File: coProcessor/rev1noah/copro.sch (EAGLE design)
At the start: 0 parts

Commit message: added several eagle libraries, all "big" parts are on the copro schematic
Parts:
- added J1: USB_MINI-B_SMT, SparkFun-Connectors:USB_MINI-B_SMT
- added J2: PJ-002AH-SMT-TR, PJ-002AH-SMT-TR:PJ-002AH-SMT-TR
- added J3: 455-1750-1-ND, SparkFun-Connectors:CONN_03
- added J4: 30320-6002HB, 30320-6002HB:30320-6002HB
- added OK1: SFH610, optocoupler:SFH610
- added P1: 503500-0991, 503500-0991:503500-0991
- added P2: 39-30-02, con-molex-mini-fit:39-30-02
- added U$1: 5530843, 5530843-6:5530843
- added U$2: STM32F4V_100PIN_GENERIC, stm32f4:STM32F4V_100PIN_GENERIC
- added U$3: DF13-4P-1.25DSA, con-hirose-df13:DF13-4P-1.25DSA
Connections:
- new net GND: U$1.GND_1, U$1.GND_2, U$1.GND_3, U$1.GND_4, U$1.GND_5, U$1.GND_6
- new net N$1: U$1.3.3V_1, U$1.3.3V_2, U$1.3.3V_3
- new net POWER: U$1.3.3V_4, U$1.3.3V_5, U$1.3.3V_6

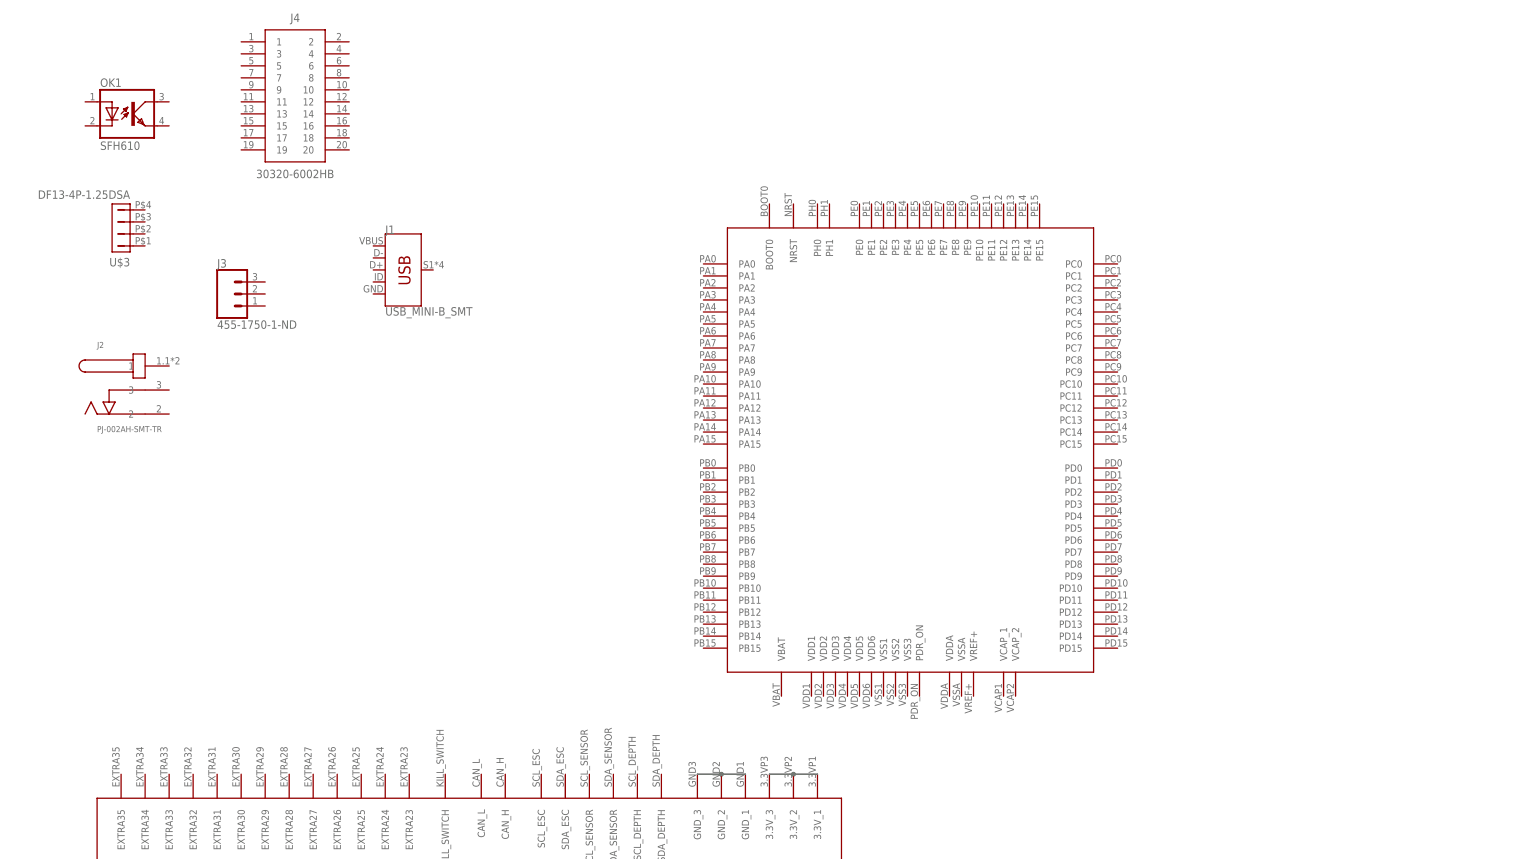
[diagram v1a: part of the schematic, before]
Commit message: some progress on the copro eagle schematic, optoisolator needs fixed
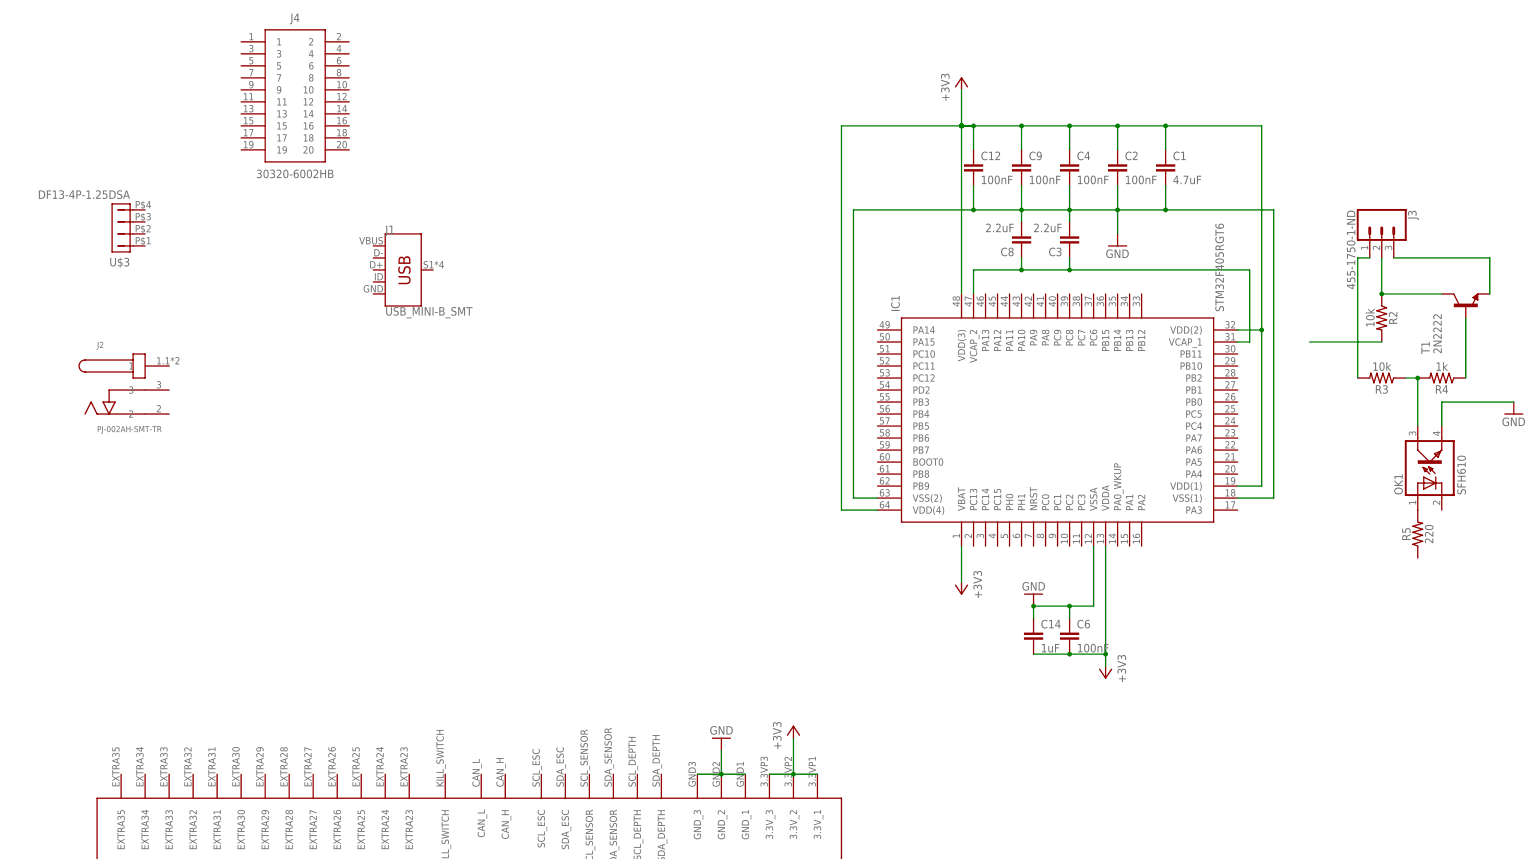
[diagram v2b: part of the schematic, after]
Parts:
- removed U$2: STM32F4V_100PIN_GENERIC, stm32f4:STM32F4V_100PIN_GENERIC
- added C1: 4.7uF, SparkFun-Capacitors:0.1UF-0603-100V-10%
- added C12, C2, C4, C6, C9: 100nF, SparkFun-Capacitors:0.1UF-0603-100V-10%
- added C14: 1uF, SparkFun-Capacitors:0.1UF-0603-100V-10%
- added C3, C8: 2.2uF, SparkFun-Capacitors:0.1UF-0603-100V-10%
- added IC1: STM32F405RGT6, STM32F405RGT6:STM32F405RGT6
- added R2, R3: 10k, SparkFun-Resistors:1KOHM-0603-1/10W-1%
- added R4: 1k, SparkFun-Resistors:1KOHM-0603-1/10W-1%
- added R5: 220, SparkFun-Resistors:1KOHM-0603-1/10W-1%
- added T1: 2N2222, transistor:2N2222
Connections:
- new net +3V3: C14.2, C6.2, IC1.VBAT, IC1.VDDA
- new net 3.3V: C1.1, C12.1, C2.1, C4.1, C9.1, IC1.VDD(1), IC1.VDD(2), IC1.VDD(3), IC1.VDD(4), U$1.3.3V_1, U$1.3.3V_2, U$1.3.3V_3
- new net N$2: R4.1, T1.B
- new net N$3: C3.1, C8.1, IC1.VCAP_1, IC1.VCAP_2
- new net N$4: OK1.A, R5.2
- new net N$5: J3.1, R3.2
- new net N$6: OK1.COL, R3.1, R4.2
- new net N$7: J3.3, T1.E
- new net N$8: R2.2
- net GND: now also C1.2, C12.2, C14.1, C2.2, C3.2, C4.2, C6.1, C8.2, C9.2, IC1.VSS(1), IC1.VSS(2), IC1.VSSA, OK1.EMIT
- net N$1: now also J3.2, R2.1, T1.C; no longer U$1.3.3V_1, U$1.3.3V_2, U$1.3.3V_3
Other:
- moved on the sheet: J3, OK1

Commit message: Opto-isolator finished, usb port finished, jtag finished
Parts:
- removed J3: 455-1750-1-ND, SparkFun-Connectors:CONN_03
- added 455-1750-1-ND, 455-1750-1-ND1, 455-1750-1-ND2, 455-1750-1-ND3, 455-1750-1-ND4, 455-1750-1-ND5, 455-1750-1-ND6, 455-1750-1-ND7, 455-1750-1-ND8, 455-1750-1-ND9: (no value), SparkFun-Connectors:CONN_03
- added OK10, OK2, OK3, OK4, OK5, OK6, OK7, OK8, OK9: SFH610, optocoupler:SFH610
- added R1, R12, R13, R16, R17, R20, R21, R24, R25, R28, R29, R32, R33, R36, R37, R40, R8, R9: 10k, SparkFun-Resistors:1KOHM-0603-1/10W-1%
- added R10, R14, R18, R22, R26, R30, R34, R38, R6: 1k, SparkFun-Resistors:1KOHM-0603-1/10W-1%
- added R11, R15, R19, R23, R27, R31, R35, R39, R7: 220, SparkFun-Resistors:1KOHM-0603-1/10W-1%
- added T10, T2, T3, T4, T5, T6, T7, T8, T9: 2N2222, transistor:2N2222
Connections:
- new net N$10: 455-1750-1-ND1.3, OK2.EMIT, T2.E
- new net N$11: OK2.A, R7.2
- new net N$12: 455-1750-1-ND1.1, R8.1, T2.C
- new net N$13: IC1.PA0_WKUP, R5.1
- new net N$14: IC1.PA1, R7.1
- new net N$15: 455-1750-1-ND1.2, R1.2, R8.2
- new net N$16: OK3.COL, R10.2, R9.1
- new net N$17: R10.1, T3.B
- new net N$18: 455-1750-1-ND2.3, OK3.EMIT, T3.E
- new net N$19: OK3.A, R11.2
- new net N$20: 455-1750-1-ND2.1, R12.1, T3.C
- new net N$21: IC1.PA2, R11.1
- new net N$22: 455-1750-1-ND2.2, R12.2, R9.2
- new net N$23: OK4.COL, R13.1, R14.2
- new net N$24: R14.1, T4.B
- new net N$25: 455-1750-1-ND3.3, OK4.EMIT, T4.E
- new net N$26: OK4.A, R15.2
- new net N$27: 455-1750-1-ND3.1, R16.1, T4.C
- new net N$28: IC1.PA3, R15.1
- new net N$29: 455-1750-1-ND3.2, R13.2, R16.2
- new net N$30: OK5.COL, R17.1, R18.2
- new net N$31: R18.1, T5.B
- new net N$32: 455-1750-1-ND4.3, OK5.EMIT, T5.E
- new net N$33: OK5.A, R19.2
- new net N$34: 455-1750-1-ND4.1, R20.1, T5.C
- new net N$35: IC1.PA6, R19.1
- new net N$36: 455-1750-1-ND4.2, R17.2, R20.2
- new net N$37: OK6.COL, R21.1, R22.2
- new net N$38: R22.1, T6.B
- new net N$39: 455-1750-1-ND5.3, OK6.EMIT, T6.E
- new net N$40: OK6.A, R23.2
- new net N$41: 455-1750-1-ND5.1, R24.1, T6.C
- new net N$42: IC1.PA7, R23.1
- new net N$43: 455-1750-1-ND5.2, R21.2, R24.2
- new net N$44: OK7.COL, R25.1, R26.2
- new net N$45: R26.1, T7.B
- new net N$46: 455-1750-1-ND6.3, OK7.EMIT, T7.E
- new net N$47: OK7.A, R27.2
- new net N$48: 455-1750-1-ND6.1, R28.1, T7.C
- new net N$49: IC1.PB0, R27.1
- new net N$50: 455-1750-1-ND6.2, R25.2, R28.2
- new net N$51: OK8.COL, R29.1, R30.2
- new net N$52: R30.1, T8.B
- new net N$53: 455-1750-1-ND7.3, OK8.EMIT, T8.E
- new net N$54: OK8.A, R31.2
- new net N$55: 455-1750-1-ND7.1, R32.1, T8.C
- new net N$56: IC1.PB1, R31.1
- new net N$57: 455-1750-1-ND7.2, R29.2, R32.2
- new net N$58: OK9.COL, R33.1, R34.2
- new net N$59: R34.1, T9.B
- new net N$60: 455-1750-1-ND8.3, OK9.EMIT, T9.E
- new net N$61: OK9.A, R35.2
- new net N$62: 455-1750-1-ND8.1, R36.1, T9.C
- new net N$63: IC1.PB10, R35.1
- new net N$64: 455-1750-1-ND8.2, R33.2, R36.2
- new net N$65: OK10.COL, R37.1, R38.2
- new net N$66: R38.1, T10.B
- new net N$67: 455-1750-1-ND9.3, OK10.EMIT, T10.E
- new net N$68: OK10.A, R39.2
- new net N$69: 455-1750-1-ND9.1, R40.1, T10.C
- new net N$70: IC1.PB11, R39.1
- new net N$71: 455-1750-1-ND9.2, R37.2, R40.2
- new net N$72: IC1.PB14, J1.D-
- new net N$73: IC1.PB15, J1.D+
- new net N$74: IC1.NRST, J4.15
- new net N$75: IC1.PB3, J4.13
- new net N$76: IC1.PA14, J4.9
- new net N$77: IC1.PA15, J4.7
- new net N$78: IC1.PA13, J4.5
- new net N$79: IC1.PB4, J4.3
- new net N$9: R6.1, T2.B
- net +3V3: now also J1.VBUS, J4.1, J4.2
- net GND: now also J1.GND, J1.SHIELD, J4.10, J4.12, J4.14, J4.16, J4.18, J4.20, J4.4, J4.6, J4.8, OK1.C, OK10.C, OK2.C, OK3.C, OK4.C, OK5.C, OK6.C, OK7.C, OK8.C, OK9.C; no longer OK1.EMIT
- net N$1: now also OK2.COL, R1.1, R6.2; no longer J3.2, R2.1, T1.C
- net N$5: now also 455-1750-1-ND.1, R2.1, T1.C; no longer J3.1, R3.2
- net N$7: now also 455-1750-1-ND.3, OK1.EMIT; no longer J3.3
- net N$8: now also 455-1750-1-ND.2, R3.2
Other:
- moved on the sheet: C1, C12, C2, C3, C4, C8, C9, J1, J4, OK1, R2, R3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

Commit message: copro board schematic nearly finished. Still need to work out transceiver
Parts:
- removed P1: 503500-0991, 503500-0991:503500-0991
- removed P2: 39-30-02, con-molex-mini-fit:39-30-02
- removed U$3: DF13-4P-1.25DSA, con-hirose-df13:DF13-4P-1.25DSA
- added DEPTH_SENSOR: DF13-4P-1.25DSA, con-hirose-df13:DF13-4P-1.25DSA
- added HEARTBEAT1, HEARTBEAT2: LTST-S270GKT, LTST-S270GKT:LTST-S270GKT
- added J3: 693061010911, 693061010911:693061010911
- added POWERJACK: PJ-002AH-SMT-TR, PJ-002AH-SMT-TR:PJ-002AH-SMT-TR
- added R41, R42: 2.2k, SparkFun-Resistors:1KOHM-0603-1/10W-1%
- added R43, R44: 330, SparkFun-Resistors:1KOHM-0603-1/10W-1%
- added RESET_SWITCH: (no value), switch:REKN
- added SWITCH1: 39-30-02, con-molex-mini-fit:39-30-02
- added U1: LM2597N-5.0, LM2597N-5.0:LM2597N-5.0
- added U2: SN65HVD232QD, SN65HVD232QD:SN65HVD232QD
- J2: value PJ-002AH-SMT-TR -> 79107-08; device PJ-002AH-SMT-TR:PJ-002AH-SMT-TR -> con-molex-milli-grid:79107-08
- renumbered OK1 to OI1, OK10 to OI10, OK2 to OI2, OK3 to OI3, OK4 to OI4, OK5 to OI5, OK6 to OI6, OK7 to OI7, OK8 to OI8, OK9 to OI9
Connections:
- net N$14 renamed OI2
- net N$21 renamed OI3
- net N$28 renamed OI4
- net N$35 renamed OI5
- net N$42 renamed OI6
- net N$49 renamed OI7
- net N$56 renamed OI8
- net N$63 renamed OIO9
- net N$7 renamed GNDBAT
- net N$70 renamed OI10
- net N$72 renamed D-
- net N$73 renamed D+
- net N$75 renamed JTAG13
- net N$76 renamed JTAG9
- net N$77 renamed PA15
- net N$78 renamed JTAG5
- net N$79 renamed JTAG3
- removed net N$34: 455-1750-1-ND4.1, R20.1, T5.C
- removed net N$39: 455-1750-1-ND5.3, OI6.EMIT, T6.E
- removed net N$41: 455-1750-1-ND5.1, R24.1, T6.C
- removed net N$46: 455-1750-1-ND6.3, OI7.EMIT, T7.E
- removed net N$48: 455-1750-1-ND6.1, R28.1, T7.C
- removed net N$53: 455-1750-1-ND7.3, OI8.EMIT, T8.E
- removed net N$55: 455-1750-1-ND7.1, R32.1, T8.C
- removed net N$60: 455-1750-1-ND8.3, OI9.EMIT, T9.E
- removed net N$62: 455-1750-1-ND8.1, R36.1, T9.C
- removed net N$67: 455-1750-1-ND9.3, OI10.EMIT, T10.E
- removed net N$69: 455-1750-1-ND9.1, R40.1, T10.C
- removed net N$74: IC1.NRST, J4.15
- new net CLK: IC1.PC12, J3.CLK
- new net CMD: IC1.PD2, J3.CMD
- new net DATO: IC1.PC8, J3.DAT0
- new net GNDA: 455-1750-1-ND1.3, 455-1750-1-ND2.3, 455-1750-1-ND3.3, 455-1750-1-ND4.3, 455-1750-1-ND5.3, 455-1750-1-ND6.3, 455-1750-1-ND7.3, 455-1750-1-ND8.3, 455-1750-1-ND9.3, OI10.EMIT, OI2.EMIT, OI3.EMIT, OI4.EMIT, OI5.EMIT, OI6.EMIT, OI7.EMIT, OI8.EMIT, OI9.EMIT, SWITCH1.1, T10.E, T2.E, T3.E, T4.E, T5.E, T6.E, T7.E, T8.E, T9.E
- new net HEARTBEAT1: IC1.PC6, R44.1
- new net HEARTBEAT2: IC1.PC7, R43.1
- new net JTAG15: IC1.NRST, J4.15, RESET_SWITCH.1@A, RESET_SWITCH.1@B
- new net N$14: HEARTBEAT2.A2, R43.2
- new net N$21: J3.GND, J3.VSS1, J3.VSS2
- new net N$28: HEARTBEAT1.A2, R44.2
- new net N$7: SWITCH1.2, U1.VIN
- new net PB8: DEPTH_SENSOR.2, IC1.PB8, R41.1
- new net PS$3: DEPTH_SENSOR.3, IC1.PB9, R42.1
- new net TXD: IC1.PA12, U2.D
- net +3V3: now also C1.1, C12.1, C2.1, C4.1, C9.1, DEPTH_SENSOR.1, IC1.VDD(1), IC1.VDD(2), IC1.VDD(3), IC1.VDD(4), J2.1, J2.3, J2.5, J2.7, J3.VDD, POWERJACK.1, R41.2, R42.2, U2.VCC; no longer IC1.VBAT
- net 3.3V: no longer C1.1, C12.1, C2.1, C4.1, C9.1, IC1.VDD(1), IC1.VDD(2), IC1.VDD(3), IC1.VDD(4)
- net GND: now also DEPTH_SENSOR.4, HEARTBEAT1.K2, HEARTBEAT2.K2, POWERJACK.2, POWERJACK.3, RESET_SWITCH.0@B, U1.GND, U2.GND
- net N$10: now also R2.2, R3.2; no longer 455-1750-1-ND1.3, OI2.EMIT, T2.E
- net N$12: now also U$1.CAN_L, U2.CANL; no longer 455-1750-1-ND1.1, R8.1, T2.C
- net N$15: no longer 455-1750-1-ND1.2
- net N$18: now also 455-1750-1-ND.1, 455-1750-1-ND1.1, 455-1750-1-ND2.1, 455-1750-1-ND3.1, 455-1750-1-ND4.1, 455-1750-1-ND5.1, 455-1750-1-ND6.1, 455-1750-1-ND7.1, 455-1750-1-ND8.1, 455-1750-1-ND9.1, R12.1, R16.1, R2.1, R20.1, R24.1, R28.1, R32.1, R36.1, R40.1, R8.1, T1.C, T10.C, T2.C, T3.C, T4.C, T5.C, T6.C, T7.C, T8.C, T9.C, U1.OUT; no longer 455-1750-1-ND2.3, OI3.EMIT, T3.E
- net N$20: now also IC1.PC0, J2.2; no longer 455-1750-1-ND2.1, R12.1, T3.C
- net N$22: no longer 455-1750-1-ND2.2
- net N$25: now also IC1.PC1, J2.4; no longer 455-1750-1-ND3.3, OI4.EMIT, T4.E
- net N$27: now also IC1.PC2, J2.6; no longer 455-1750-1-ND3.1, R16.1, T4.C
- net N$29: no longer 455-1750-1-ND3.2
- net N$32: now also IC1.PC3, J2.8; no longer 455-1750-1-ND4.3, OI5.EMIT, T5.E
- net N$36: no longer 455-1750-1-ND4.2
- net N$43: no longer 455-1750-1-ND5.2
- net N$5: now also IC1.PA11, U2.R; no longer 455-1750-1-ND.1, R2.1, T1.C
- net N$50: no longer 455-1750-1-ND6.2
- net N$57: no longer 455-1750-1-ND7.2
- net N$64: no longer 455-1750-1-ND8.2
- net N$71: no longer 455-1750-1-ND9.2
- net N$8: now also U$1.CAN_H, U2.CANH; no longer 455-1750-1-ND.2, R2.2, R3.2
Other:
- note added: "18 - 22 V"
- note added: "5 v"
- note added: "NEEDS WORK"
- moved on the sheet: C1, C12, C14, C2, C3, C4, C6, C8, C9
